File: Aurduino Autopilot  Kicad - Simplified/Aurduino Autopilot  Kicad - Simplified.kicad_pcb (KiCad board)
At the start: 2 copper layers, 76 x 74 mm, 26 parts, among them J1 12V_in, J2 to_clock, J3 to_LCD, J5 to_RTC, SW1 SW_Push, U1 LM350_TO3

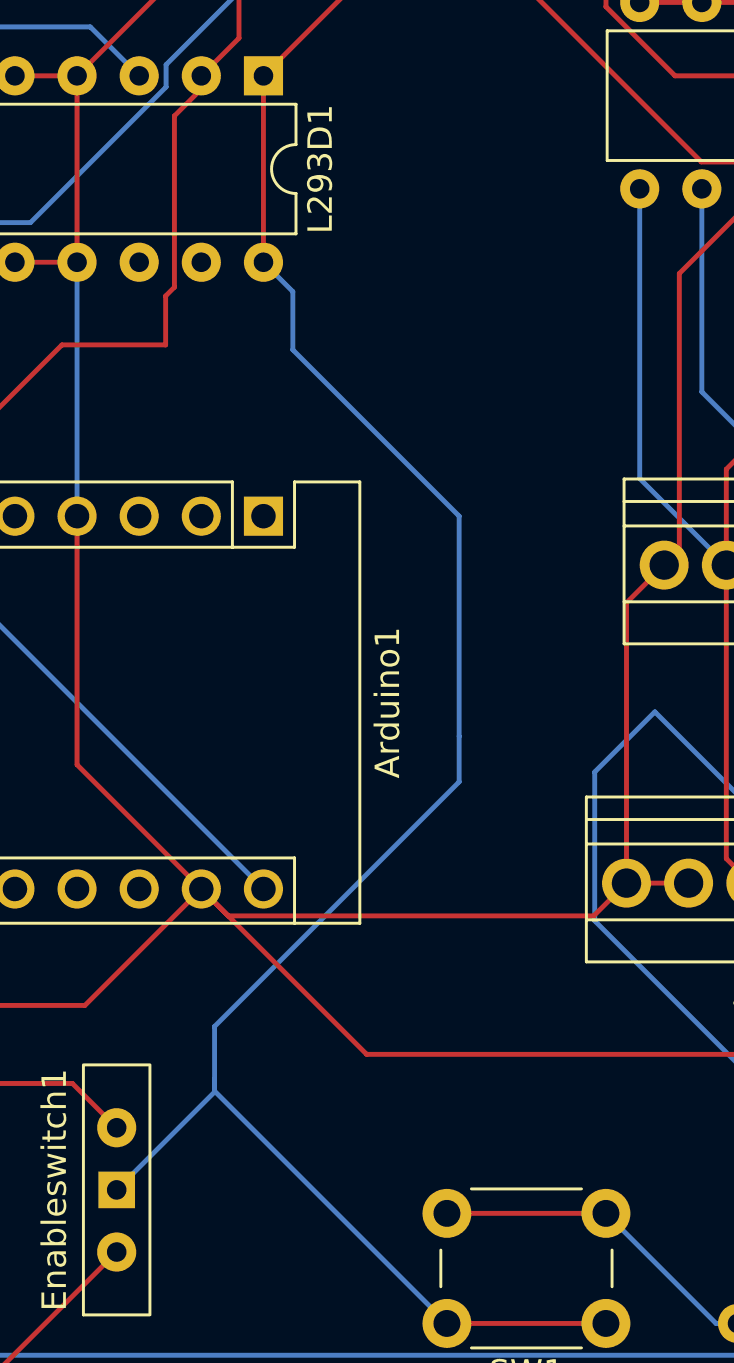
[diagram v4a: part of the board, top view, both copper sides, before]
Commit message: fixed hanging wire
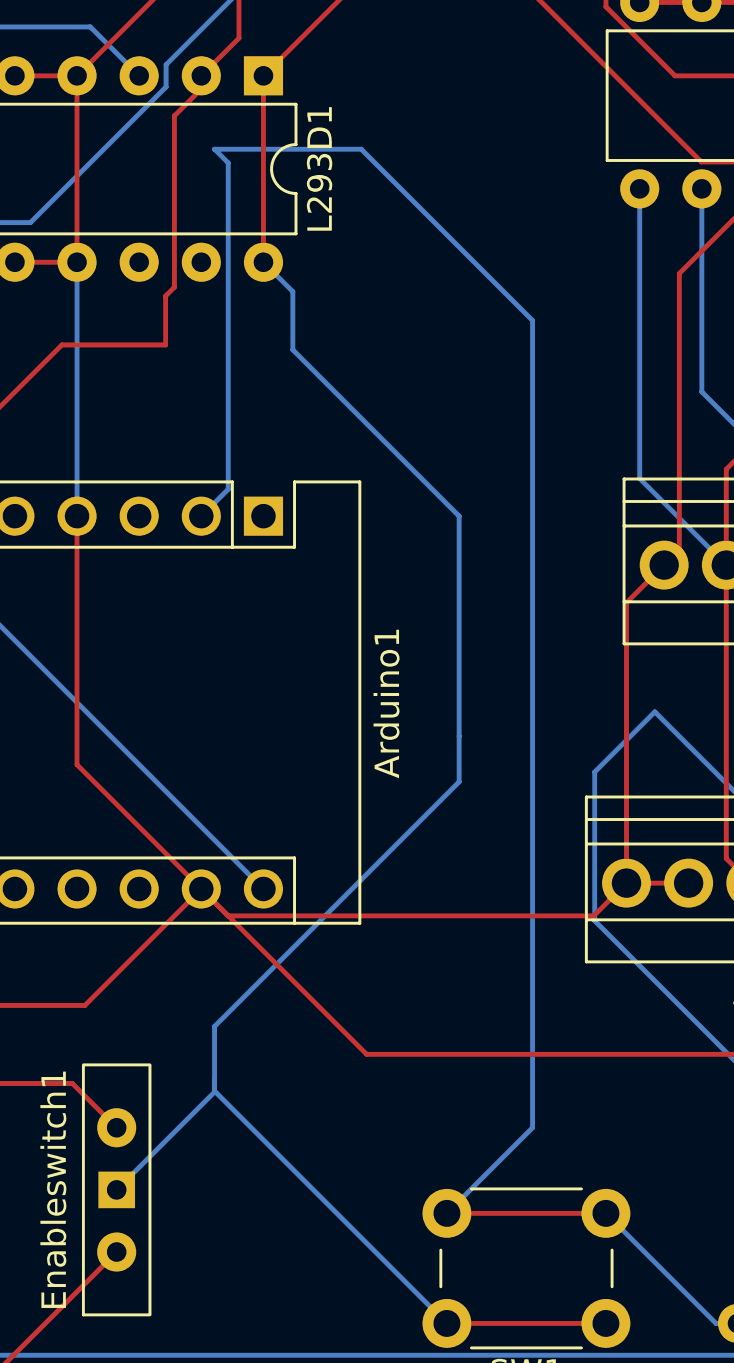
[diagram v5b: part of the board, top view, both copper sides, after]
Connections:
- Arduino1 pad 2: unconnected-(Arduino1-D0/RX-Pad2) -> Net-(Arduino1-D0/RX)
- SW1 pad 2: Net-(SW1-Pad2) -> Net-(Arduino1-D0/RX)
- pd_ib1 pad 1: Net-(SW1-Pad2) -> Net-(Arduino1-D0/RX)
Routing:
- net Net-(Arduino1-D0/RX): track 0.00 -> 83.3 mm
- net Net-(SW1-Pad2): track 13.7 -> 0.00 mm
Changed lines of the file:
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@@
 	(net 36 "unconnected-(Arduino1-D1{slash}TX-Pad1)")
 	(net 37 "Net-(Arduino1-D3)")
-	(net 38 "unconnected-(Arduino1-D0{slash}RX-Pad2)")
+	(net 38 "Net-(Arduino1-D0{slash}RX)")
 	(net 39 "Net-(Arduino1-A5)")
-	(net 40 "Net-(SW1-Pad2)")
-	(net 41 "Net-(U1-ADJ)")
+	(net 40 "Net-(U1-ADJ)")
 	(footprint "Connector_Wire:SolderWire-1sqmm_1x02_P5.4mm_D1.4mm_OD2.7mm"
 		(layer "F.Cu")
@@
 			(layers "*.Cu" "*.Mask")
 			(remove_unused_layers no)
-			(net 40 "Net-(SW1-Pad2)")
+			(net 38 "Net-(Arduino1-D0{slash}RX)")
 			(pintype "passive")
 		)
@@
 			(layers "*.Cu" "*.Mask")
 			(remove_unused_layers no)
-			(net 41 "Net-(U1-ADJ)")
+			(net 40 "Net-(U1-ADJ)")
 			(pintype "passive")
 		)
@@
 			(layers "*.Cu" "*.Mask")
 			(remove_unused_layers no)
-			(net 41 "Net-(U1-ADJ)")
+			(net 40 "Net-(U1-ADJ)")
 			(pinfunction "ADJ")
 			(pintype "input")
@@
 			(layers "*.Cu" "*.Mask")
 			(remove_unused_layers no)
-			(net 38 "unconnected-(Arduino1-D0{slash}RX-Pad2)")
+			(net 38 "Net-(Arduino1-D0{slash}RX)")
 			(pinfunction "D0/RX")
 			(pintype "bidirectional")
@@
 			(layers "*.Cu" "*.Mask")
 			(remove_unused_layers no)
-			(net 40 "Net-(SW1-Pad2)")
+			(net 38 "Net-(Arduino1-D0{slash}RX)")
 			(pinfunction "2")
 			(pintype "passive")
@@
 			(layers "*.Cu" "*.Mask")
 			(remove_unused_layers no)
-			(net 40 "Net-(SW1-Pad2)")
+			(net 38 "Net-(Arduino1-D0{slash}RX)")
 			(pinfunction "2")
 			(pintype "passive")
@@
 			(layers "*.Cu" "*.Mask")
 			(remove_unused_layers no)
-			(net 41 "Net-(U1-ADJ)")
+			(net 40 "Net-(U1-ADJ)")
 			(pintype "passive")
 		)
@@
 	)
 	(segment
+		(start 79.5 115.5)
+		(end 86 115.5)
+		(width 0.2)
+		(layer "F.Cu")
+		(net 38)
+	)
+	(segment
+		(start 76 72)
+		(end 83 79)
+		(width 0.2)
+		(layer "B.Cu")
+		(net 38)
+	)
+	(segment
+		(start 83 79)
+		(end 83 112)
+		(width 0.2)
+		(layer "B.Cu")
+		(net 38)
+	)
+	(segment
+		(start 86 115.5)
+		(end 90.5 120)
+		(width 0.2)
+		(layer "B.Cu")
+		(net 38)
+	)
+	(segment
+		(start 70.56 72.56)
+		(end 70 72)
+		(width 0.2)
+		(layer "B.Cu")
+		(net 38)
+	)
+	(segment
+		(start 69.46 87)
+		(end 70.56 85.9)
+		(width 0.2)
+		(layer "B.Cu")
+		(net 38)
+	)
+	(segment
+		(start 70 72)
+		(end 76 72)
+		(width 0.2)
+		(layer "B.Cu")
+		(net 38)
+	)
+	(segment
+		(start 70.56 85.9)
+		(end 70.56 72.56)
+		(width 0.2)
+		(layer "B.Cu")
+		(net 38)
+	)
+	(segment
+		(start 83 112)
+		(end 79.5 115.5)
+		(width 0.2)
+		(layer "B.Cu")
+		(net 38)
+	)
+	(segment
+		(start 90.5 120)
+		(end 91.38 120)
+		(width 0.2)
+		(layer "B.Cu")
+		(net 38)
+	)
+	(segment
 		(start 94.46 90)
 		(end 94.46 102)
@@
 	)
 	(segment
-		(start 79.5 115.5)
-		(end 86 115.5)
-		(width 0.2)
-		(layer "F.Cu")
-		(net 40)
-	)
-	(segment
-		(start 86 115.5)
-		(end 90.5 120)
-		(width 0.2)
-		(layer "B.Cu")
-		(net 40)
-	)
-	(segment
-		(start 90.5 120)
-		(end 91.38 120)
-		(width 0.2)
-		(layer "B.Cu")
-		(net 40)
-	)
-	(segment
 		(start 46.38 63)
 		(end 56.62 63)
 		(width 0.2)
 		(layer "F.Cu")
-		(net 41)
+		(net 40)
 	)
 	(segment
@@
 		(width 0.2)
 		(layer "F.Cu")
-		(net 41)
+		(net 40)
 	)
 	(segment
@@
 		(width 0.2)
 		(layer "F.Cu")
-		(net 41)
+		(net 40)
 	)
 	(segment
@@
 		(width 0.2)
 		(layer "F.Cu")
-		(net 41)
+		(net 40)
 	)
 	(segment
@@
 		(width 0.2)
 		(layer "F.Cu")
-		(net 41)
+		(net 40)
 	)
 )
